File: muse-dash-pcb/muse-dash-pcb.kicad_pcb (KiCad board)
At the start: 2 copper layers, 84.1 x 47.3 mm, 24 parts, among them SW0 SW_Push, SW1 CherryMX, SW2 CherryMX, SW3 CherryMX, SW4 CherryMX, U1 ATmega32U4-A, Y1 Crystal_GND24

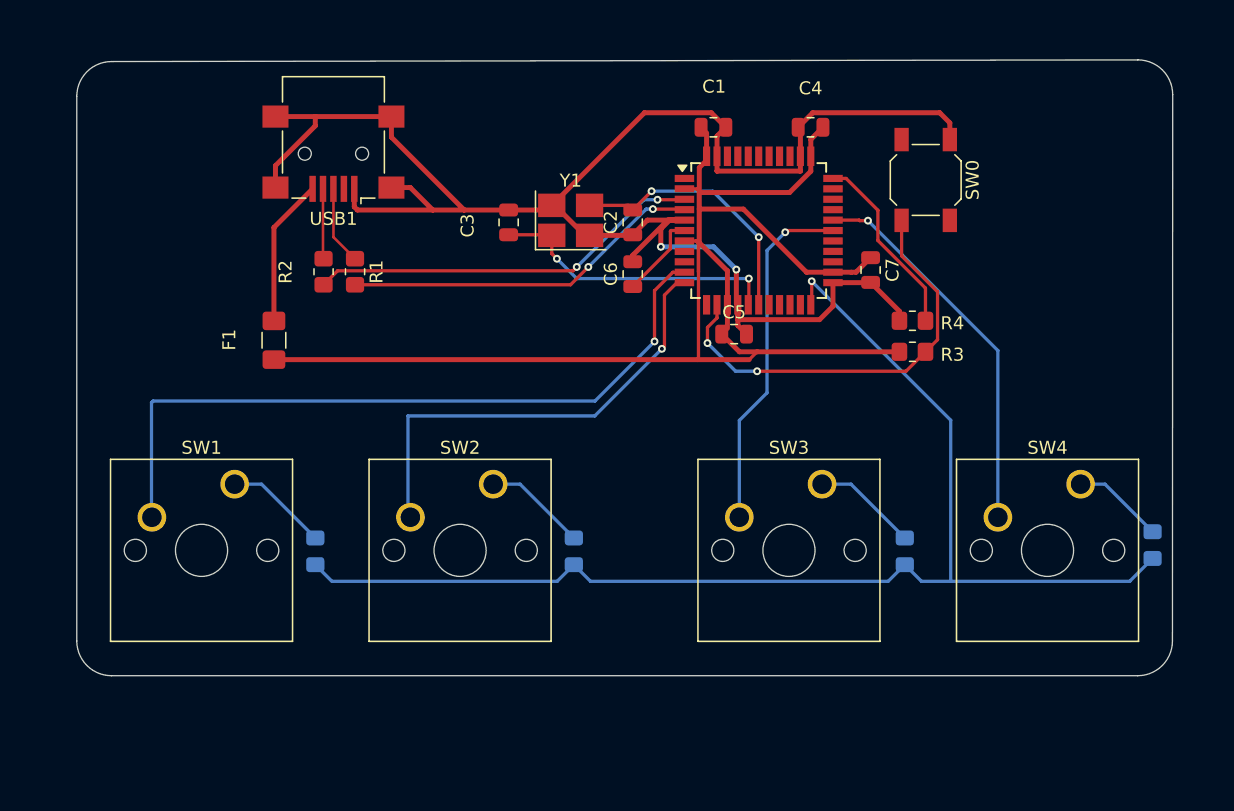
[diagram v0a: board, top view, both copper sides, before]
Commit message: fixed routes and added mounting holes
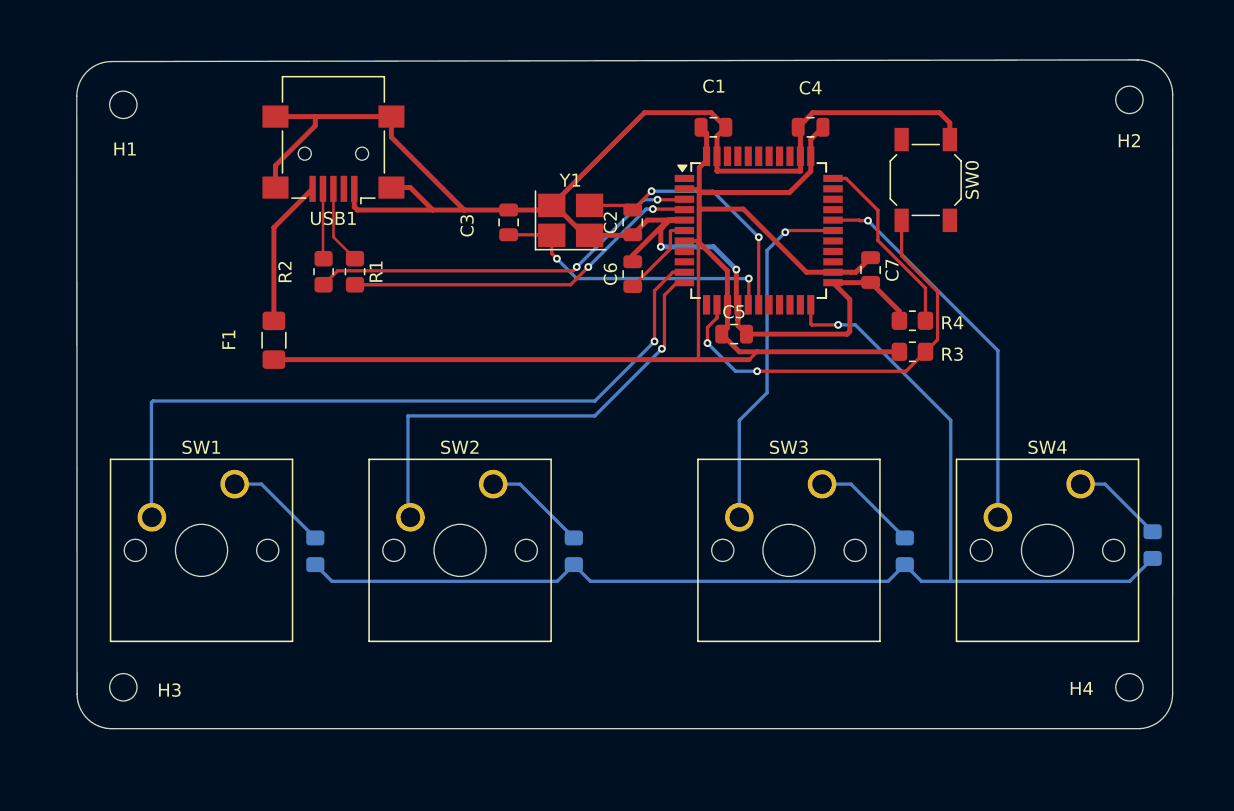
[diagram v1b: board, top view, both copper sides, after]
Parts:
- added H1: MountingHole, MountingHole:MountingHole_2.1mm, F.Cu at (156.7, 54.9)
- added H2: MountingHole, MountingHole:MountingHole_2.1mm, F.Cu at (233.9, 54.5)
- added H3: MountingHole, MountingHole:MountingHole_2.1mm, F.Cu at (156.7, 99.6)
- added H4: MountingHole, MountingHole:MountingHole_2.1mm, F.Cu at (233.9, 99.6)
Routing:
- net GND: track 139.6 -> 142.4 mm
- net COM: track 96.9 -> 95.4 mm
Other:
- board size 84.1 x 47.3 mm -> 84.1 x 51.3 mm
- board text added: "@hominum0447"

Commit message: added ISP Interface
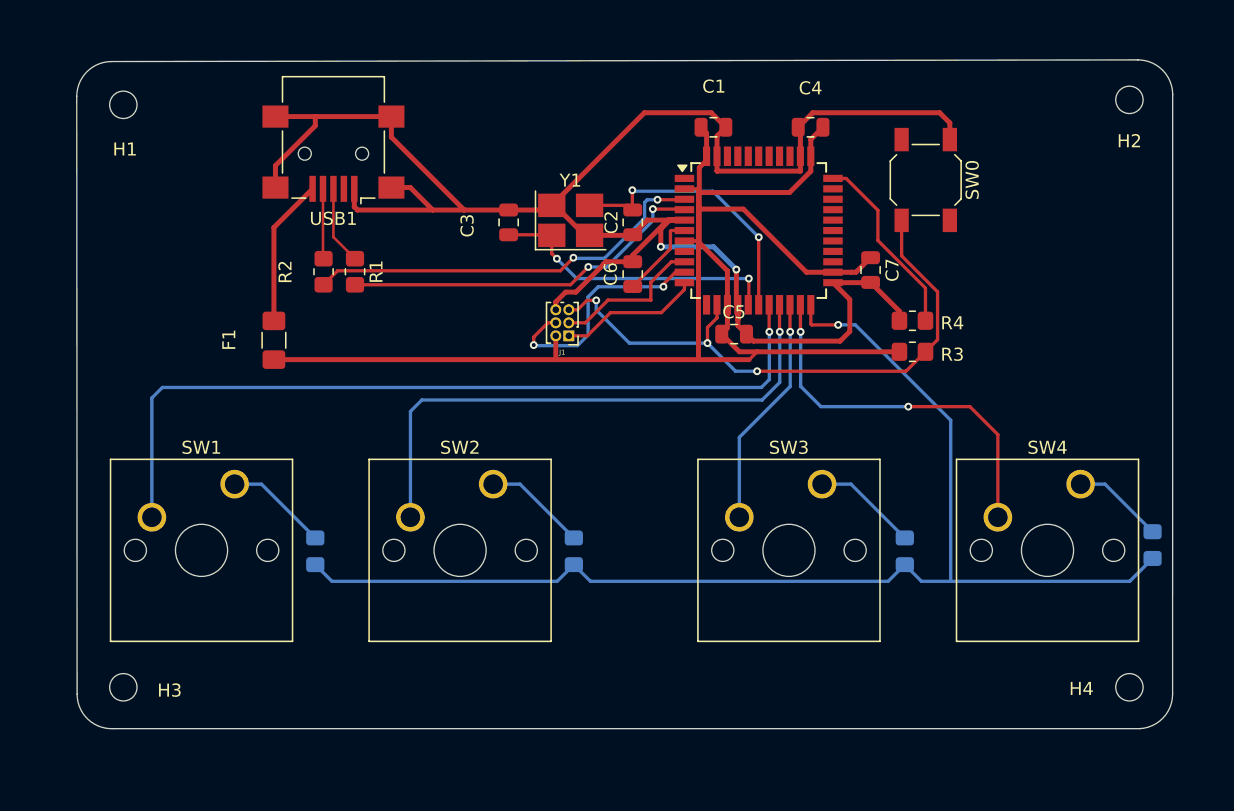
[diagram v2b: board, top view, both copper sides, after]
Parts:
- added J1: AVR-ISP-6, Connector_PinHeader_1.00mm:PinHeader_2x03_P1.00mm_Vertical, F.Cu at (190.9, 72.6)
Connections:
- net Net-(U1-~{RESET}) renamed RESET
- U1 pad 10: SW1 -> MOSI
- U1 pad 11: SW2 -> MISO
- U1 pad 18: unconnected-(U1-PD0-Pad18) -> SW1
- U1 pad 19: unconnected-(U1-PD1-Pad19) -> SW2
- U1 pad 20: unconnected-(U1-PD2-Pad20) -> SW3
- U1 pad 21: unconnected-(U1-PD3-Pad21) -> SW4
- U1 pad 28: SW3 -> unconnected-(U1-PB4-Pad28)
- U1 pad 29: SW4 -> unconnected-(U1-PB5-Pad29)
- U1 pad 9: unconnected-(U1-PB1-Pad9) -> SCK
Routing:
- net MOSI: track 0.00 -> 18.5 mm, vias 0 -> 2
- net RESET: track 33.1 -> 45.8 mm, vias 2 -> 3
- net SCK: track 0.00 -> 11.6 mm
- net MISO: track 0.00 -> 10.9 mm
- net SW3: track 27.1 -> 17.9 mm
- net GND: track 142.4 -> 150.6 mm
- net SW2: track 35.6 -> 43.4 mm
- net SW1: track 56.1 -> 62.9 mm
- net +5V: track 115.0 -> 116.9 mm
- net Net-(U1-XTAL1): track 20.4 -> 21.4 mm
- net Net-(U1-D-): track 30.4 -> 31.2 mm
- net Net-(U1-D+): track 27.7 -> 28.2 mm
- net SW4: track 29.6 -> 29.3 mm, vias 1 -> 2

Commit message: added underglow LEDs
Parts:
- added C8: 0.1uF, Capacitor_SMD:C_0805_2012Metric, B.Cu at (160.2, 67.1)
- added C9: 0.1uF, Capacitor_SMD:C_0805_2012Metric, B.Cu at (230.3, 67.6)
- added D5: WS2812B, LED_SMD:LED_WS2812B_PLCC4_5.0x5.0mm_P3.2mm, B.Cu at (160.2, 73.3)
- added D6: WS2812B, LED_SMD:LED_WS2812B_PLCC4_5.0x5.0mm_P3.2mm, B.Cu at (230.2, 73.2)
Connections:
- D1 pad 1: COM -> GND
- D2 pad 1: COM -> GND
- D3 pad 1: COM -> GND
- D4 pad 1: COM -> GND
- U1 pad 12: unconnected-(U1-PB7-Pad12) -> UNDERGLOW
- U1 pad 22: COM -> unconnected-(U1-PD5-Pad22)
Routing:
- net GND: track 150.6 -> 290.6 mm, vias 2 -> 5
- net COM: track 95.4 -> 0.00 mm, vias 1 -> 0
- net Net-(D5-DOUT): track 0.00 -> 75.4 mm
- net UNDERGLOW: track 0.00 -> 51.5 mm, vias 0 -> 1
- net +5V: track 116.9 -> 156.8 mm, vias 0 -> 4

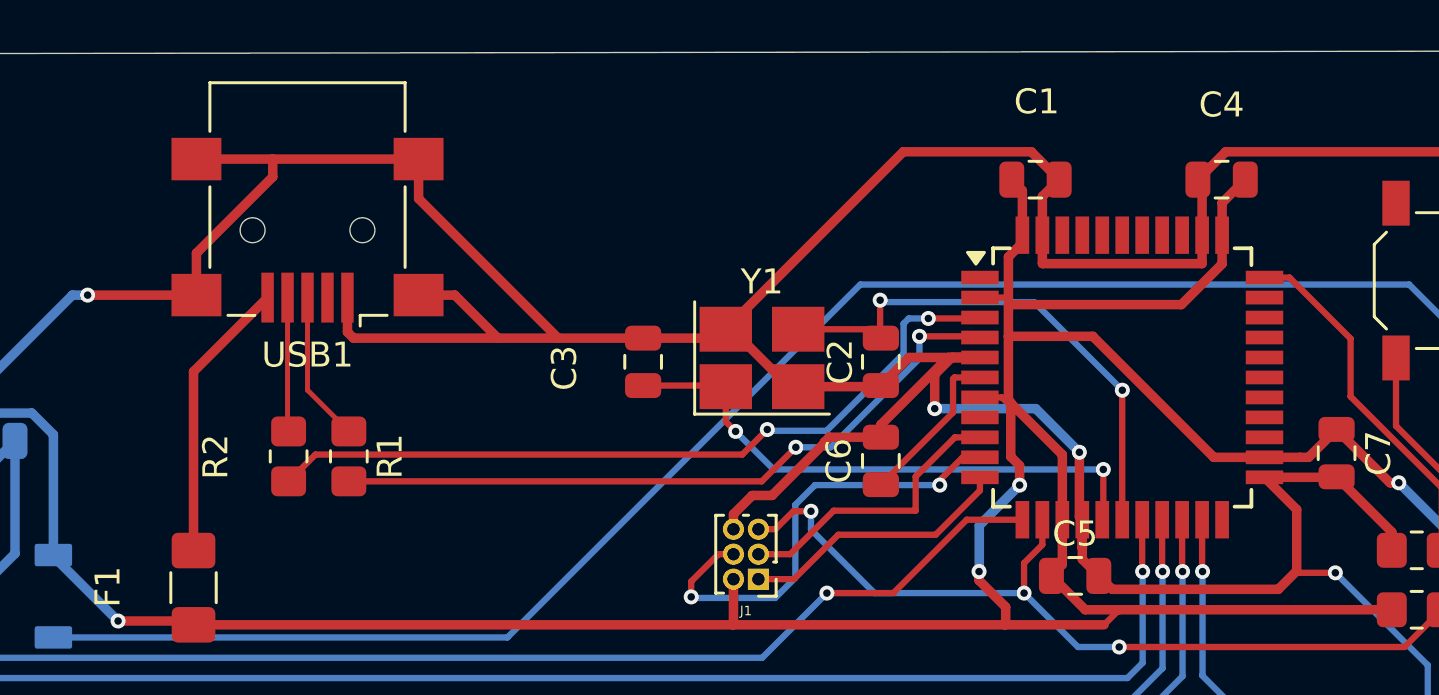
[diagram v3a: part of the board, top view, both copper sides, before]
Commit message: added ground fills
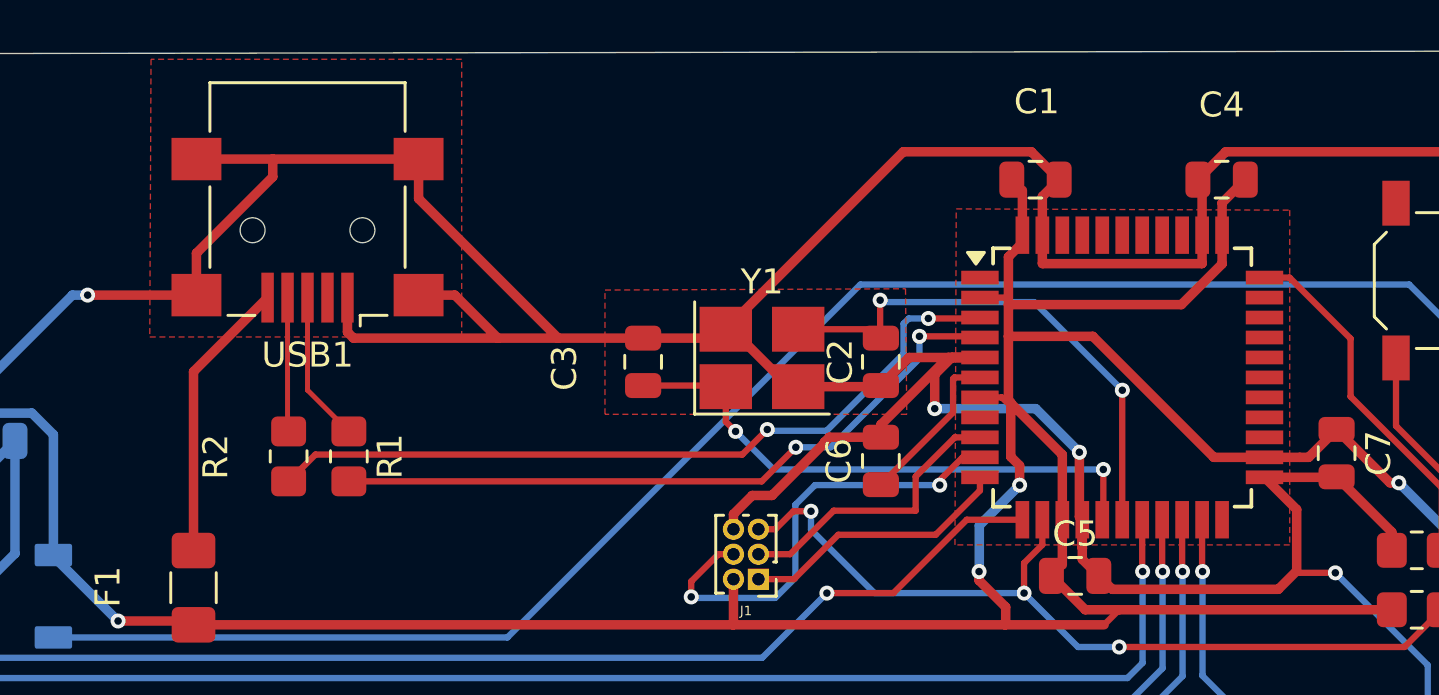
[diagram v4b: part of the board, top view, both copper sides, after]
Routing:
- added copper zone on F.Cu, net GND
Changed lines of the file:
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@@
 		(net 43)
 	)
+	(zone
+		(net 2)
+		(net_name "GND")
+		(layer "F.Cu")
+		(name "USB GND FILL")
+		(hatch edge 0.5)
+		(priority 1)
+		(connect_pads
+			(clearance 0.5)
+		)
+		(min_thickness 0.25)
+		(filled_areas_thickness no)
+		(fill
+			(thermal_gap 0.5)
+			(thermal_bridge_width 0.5)
+		)
+		(polygon
+			(pts
+				(xy 166.5732 51.7652) (xy 166.5224 62.8904) (xy 179.0192 62.8904) (xy 179.0192 51.7652)
+			)
+		)
+	)
+	(zone
+		(net 2)
+		(net_name "GND")
+		(layer "F.Cu")
+		(name "OSC GND FILL")
+		(hatch edge 0.5)
+		(priority 2)
+		(connect_pads
+			(clearance 0.5)
+		)
+		(min_thickness 0.25)
+		(filled_areas_thickness no)
+		(fill
+			(thermal_gap 0.5)
+			(thermal_bridge_width 0.5)
+		)
+		(polygon
+			(pts
+				(xy 184.7596 61.0108) (xy 196.7992 60.96) (xy 196.85 65.9892) (xy 184.7596 65.9892)
+			)
+		)
+	)
+	(zone
+		(net 2)
+		(net_name "GND")
+		(layer "F.Cu")
+		(name "MCU GND FILL")
+		(hatch edge 0.5)
+		(connect_pads
+			(clearance 0.5)
+		)
+		(min_thickness 0.25)
+		(filled_areas_thickness no)
+		(fill
+			(thermal_gap 0.5)
+			(thermal_bridge_width 0.5)
+		)
+		(polygon
+			(pts
+				(xy 198.8312 57.7596) (xy 212.1916 57.8104) (xy 212.1916 71.2216) (xy 198.7804 71.2216)
+			)
+		)
+	)
 )

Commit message: cleaned up routing
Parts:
- R3: value R -> 10K
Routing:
- net +5V: track 156.8 -> 129.9 mm, vias 4 -> 2
- net GND: track 290.6 -> 314.8 mm, vias 5 -> 4
- net Net-(D5-DOUT): track 75.4 -> 82.9 mm
- net RESET: track 45.8 -> 52.0 mm
- net SW1: track 62.9 -> 57.7 mm
- net SW4: track 29.3 -> 26.5 mm, vias 2 -> 1
- removed copper zone on F.Cu, net GND

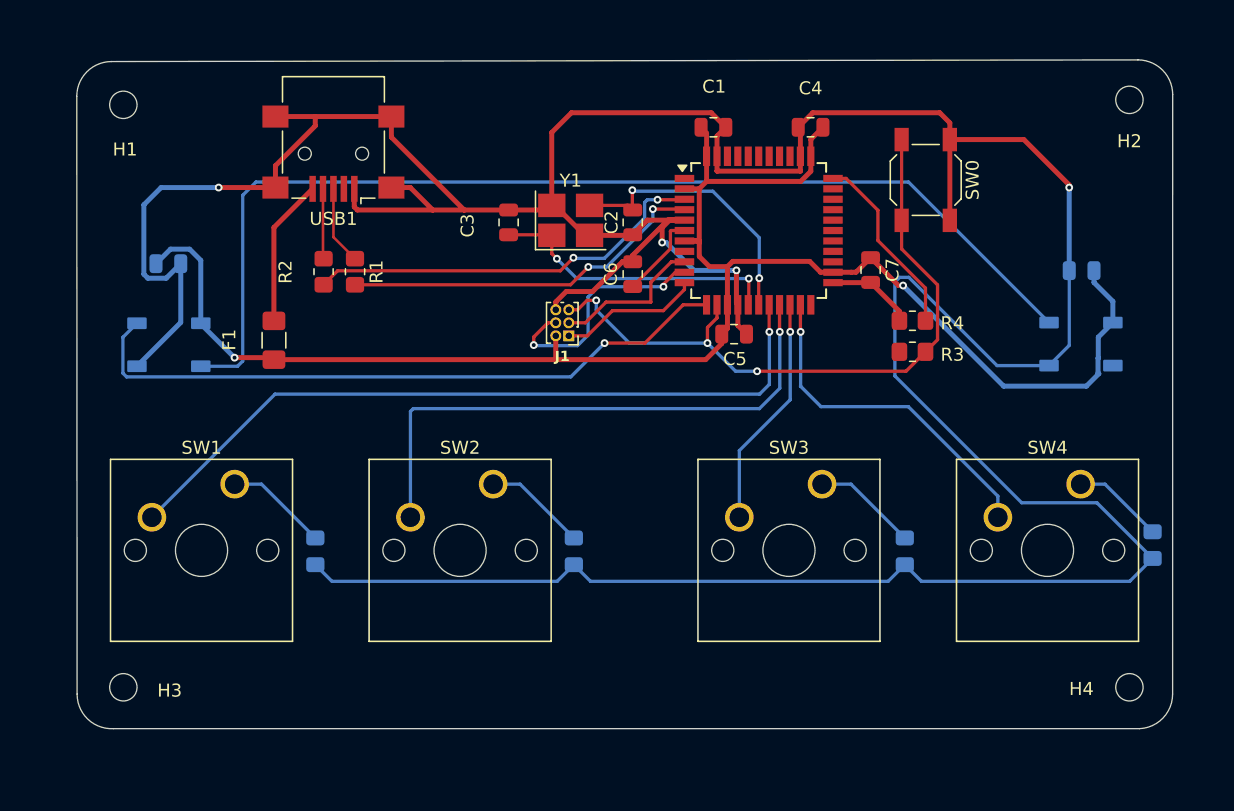
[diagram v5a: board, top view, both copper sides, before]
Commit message: changed ISP header footprint, fixed Ground plane and improved routing
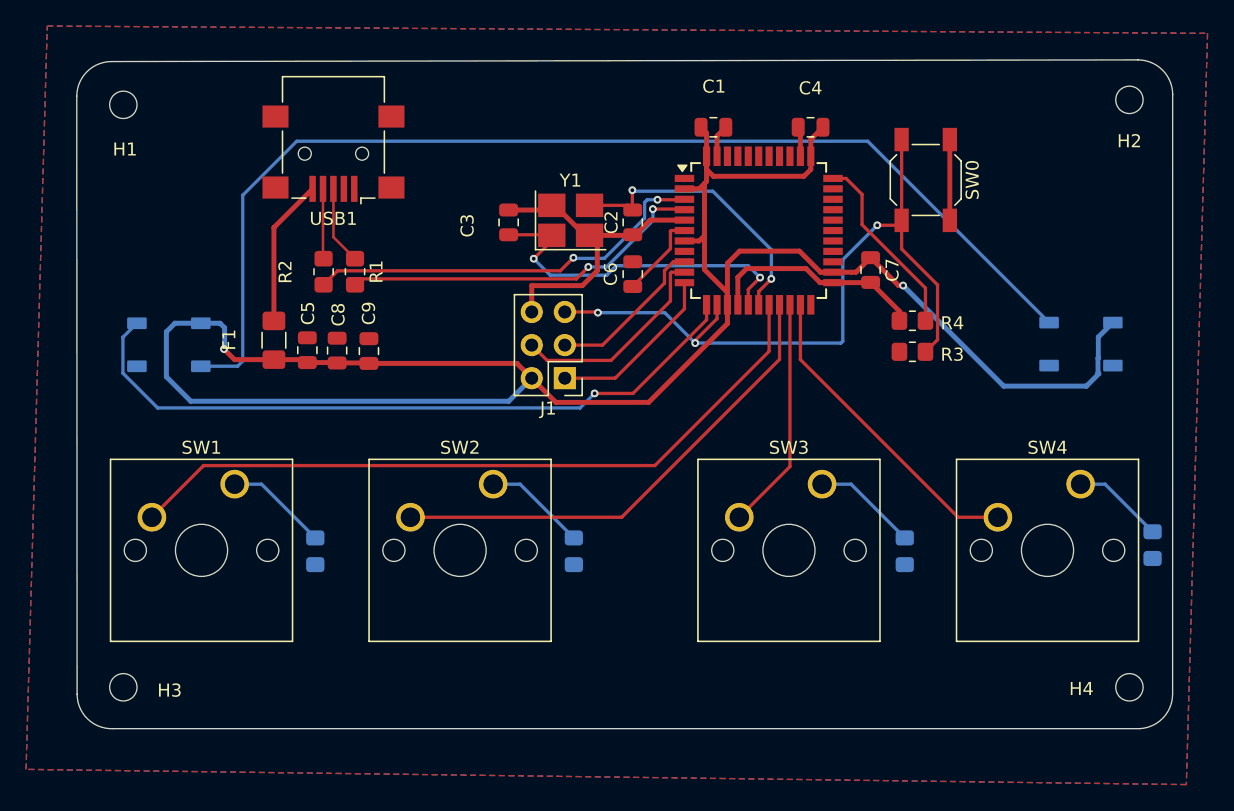
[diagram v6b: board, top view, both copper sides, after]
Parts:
- C8, C9: moved to F.Cu
- J1: footprint Connector_PinHeader_1.00mm:PinHeader_2x03_P1.00mm_Vertical -> Connector_PinHeader_2.54mm:PinHeader_2x03_P2.54mm_Vertical
- moved C9 55.0 mm to (175.6, 73.8), turned to 90 degrees
- moved C5 32.8 mm to (170.8, 73.7), turned to 90 degrees
- moved C8 14.6 mm to (173.1, 73.7), turned to -90 degrees
- moved J1 3.27 mm to (190.6, 75.8)
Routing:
- net GND: track 314.8 -> 53.5 mm, vias 4 -> 0
- net +5V: track 129.9 -> 157.0 mm
- net SW2: track 43.6 -> 37.5 mm, vias 1 -> 0
- net Net-(U1-XTAL2): track 22.7 -> 26.7 mm
- net RESET: track 52.0 -> 55.8 mm
- net UNDERGLOW: track 51.5 -> 54.1 mm
- net Net-(D5-DOUT): track 82.9 -> 85.5 mm
- net MISO: track 10.9 -> 13.4 mm
- net MOSI: track 18.5 -> 16.3 mm, vias 2 -> 0
- net SW4: track 26.5 -> 24.4 mm, vias 1 -> 0
- net SW1: track 57.7 -> 56.2 mm, vias 1 -> 0
- net Net-(U1-XTAL1): track 21.4 -> 22.2 mm
- net SCK: track 11.7 -> 12.4 mm
- net SW3: track 18.0 -> 17.9 mm, vias 1 -> 0
- added copper zone on B.Cu, net GND
- added copper zone on F.Cu, net GND

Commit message: changed oscillator footprint
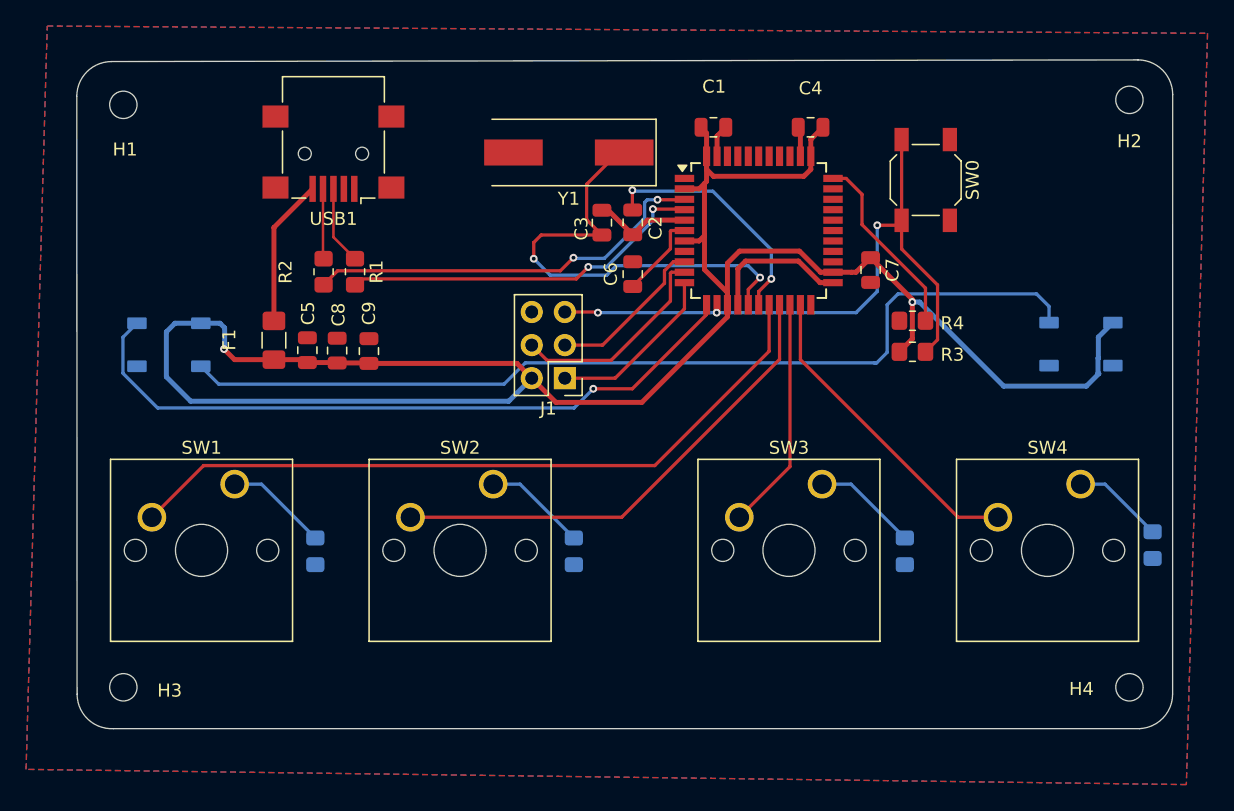
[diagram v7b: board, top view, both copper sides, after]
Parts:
- Y1: footprint Crystal:Crystal_SMD_3225-4Pin_3.2x2.5mm_HandSoldering -> Crystal:Crystal_SMD_HC49-SD
- moved C3 7.16 mm to (193.4, 63.9)
- moved Y1 5.21 mm to (190.9, 58.5), turned to 180 degrees
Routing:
- net GND: track 53.5 -> 23.4 mm
- net Net-(D5-DOUT): track 85.5 -> 72.3 mm
- net Net-(U1-XTAL2): track 26.7 -> 36.0 mm
- net RESET: track 55.8 -> 50.2 mm
- net +5V: track 157.0 -> 161.1 mm
- net Net-(U1-XTAL1): track 22.2 -> 19.2 mm
